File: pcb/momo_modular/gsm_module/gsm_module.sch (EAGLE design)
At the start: 19 parts, among them U1 PIC16LF1823, U2 TI-HIGHSIDE-PFET, U3 SIM900, U4 ESD-SMF05C

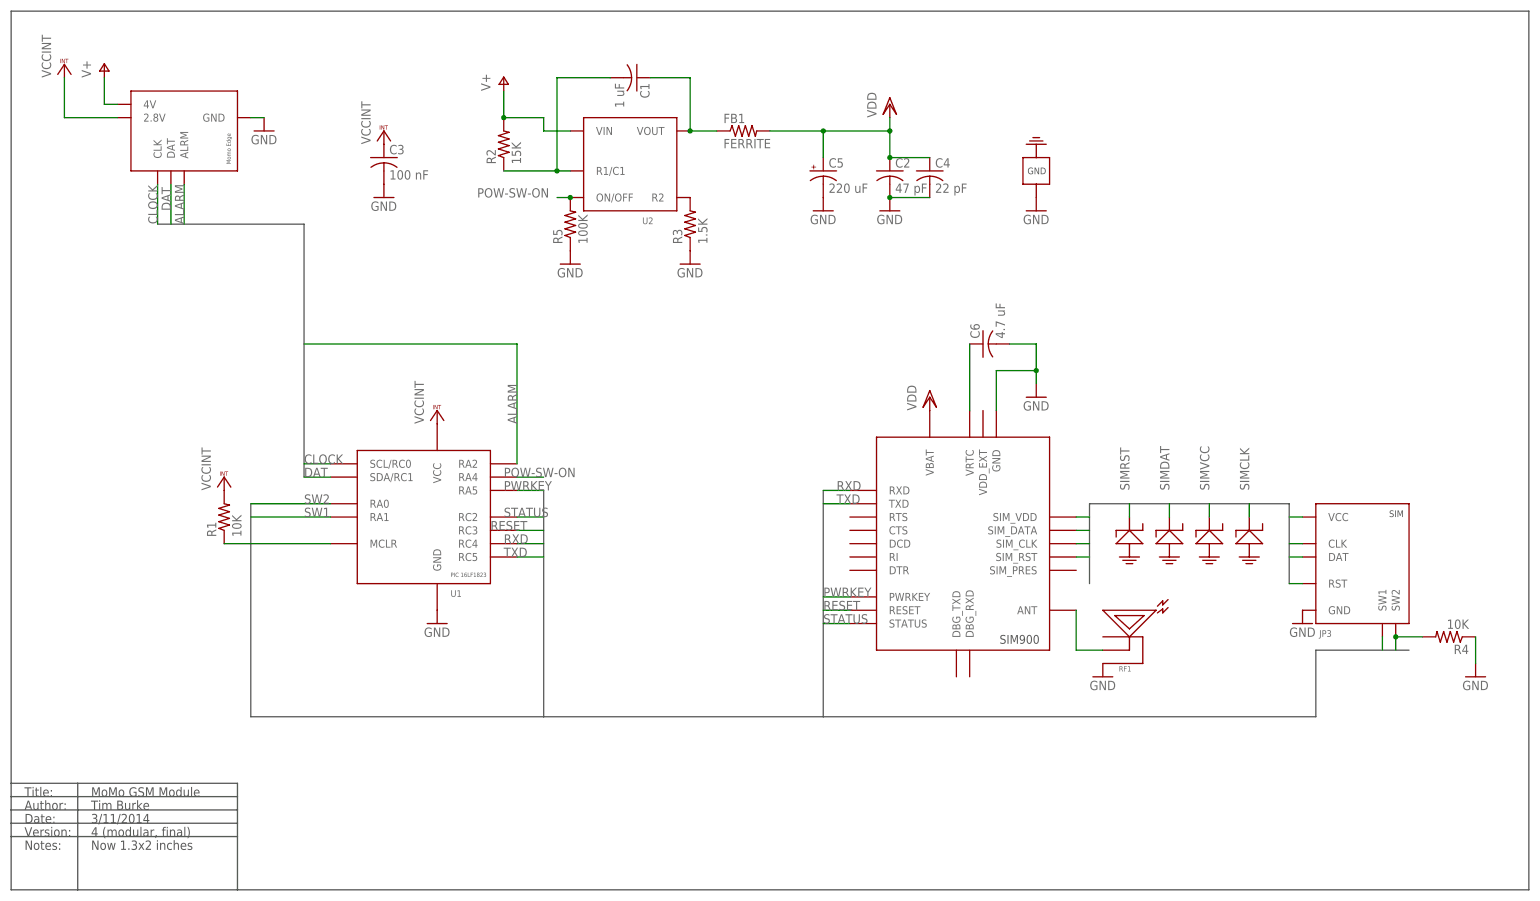
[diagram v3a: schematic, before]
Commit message: Revise GSM module to include pic16lf1847, microsim
Also updated layout for better reflow and moved
traces further from board edges.
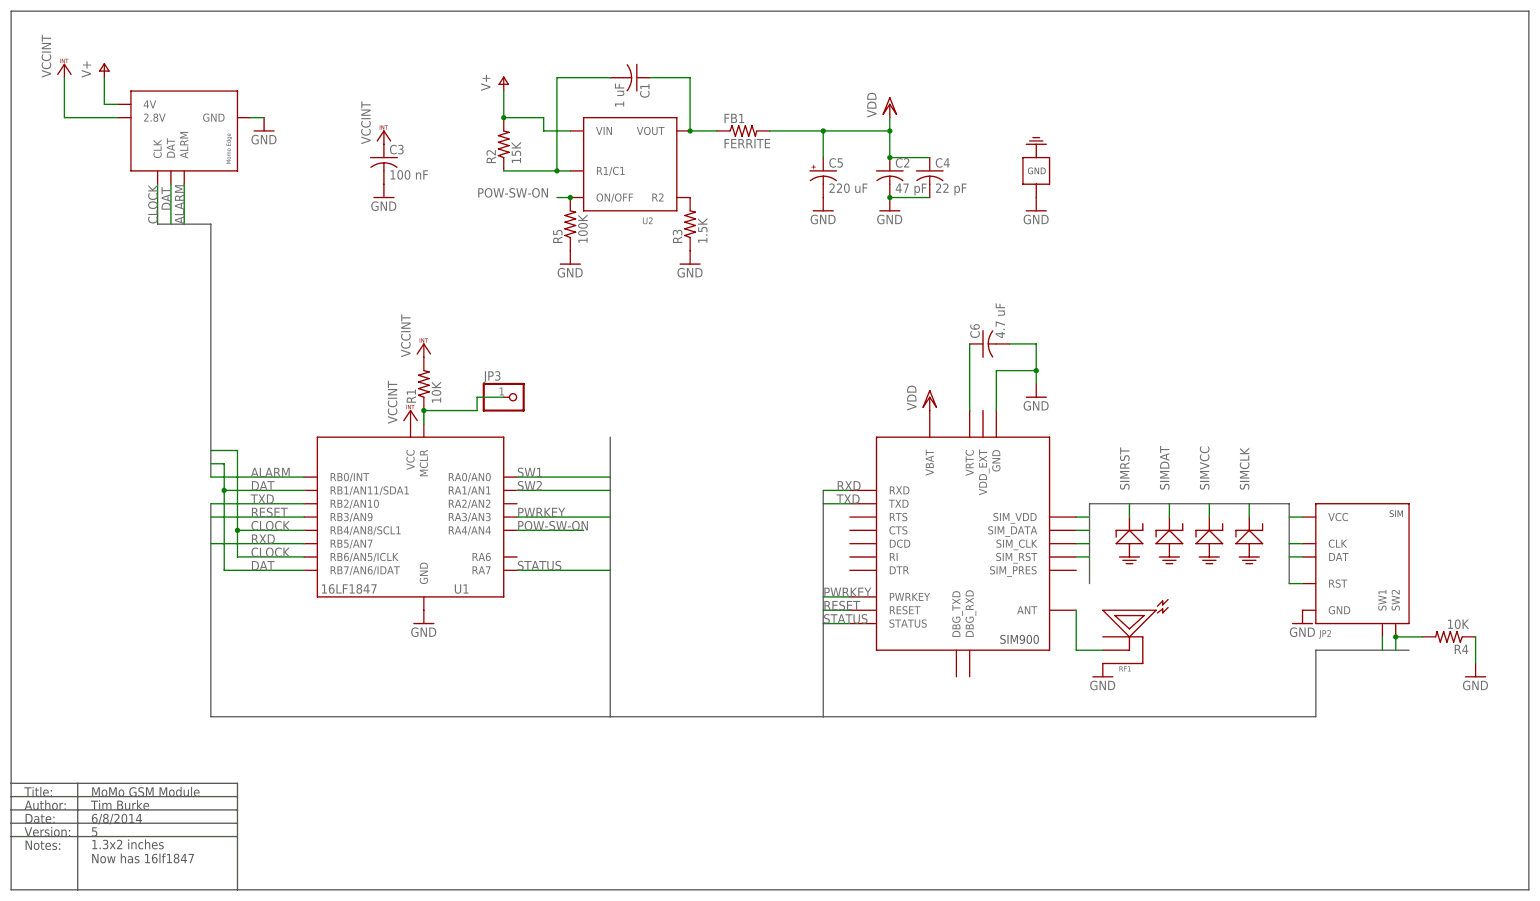
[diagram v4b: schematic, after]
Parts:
- added JP2: SIMHOLDER-8PINMICROSIM, components:SIMHOLDER-8PINMICROSIM
- JP3: value SIMHOLDER-8PINHING -> (none); device components:SIMHOLDER-8PINHING -> pinhead:PINHD-1X1
- U1: value PIC16LF1823 -> PIC16LF1847; device components:PIC16LF1823 -> components:PIC16LF1847; DIGIKEY-PN PIC16LF1823-I/SL-ND -> (none)
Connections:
- removed net N$6: R1.1, U1.MCLR
- new net N$2: JP3.1, R1.1, U1.MCLR
- net ALARM: now also U1.RB0/INT; no longer U1.RA2
- net CLOCK: now also U1.RB4/AN8/SCL1, U1.RB6/AN5/ICLK; no longer U1.SCL/RC0
- net DAT: now also U1.RB1/AN11/SDA1, U1.RB7/AN6/IDAT; no longer U1.SDA/RC1
- net GND: now also JP2.GND; no longer JP3.GND
- net POW-SW-ON: now also U1.RA4/AN4; no longer U1.RA4
- net PWRKEY: now also U1.RA3/AN3; no longer U1.RA5
- net RESET: now also U1.RB3/AN9; no longer U1.RC3
- net RXD: now also U1.RB5/AN7; no longer U1.RC4
- net SIMCLK: now also JP2.CLK; no longer JP3.CLK
- net SIMDAT: now also JP2.DAT; no longer JP3.DAT
- net SIMRST: now also JP2.RST; no longer JP3.RST
- net SIMVCC: now also JP2.VCC; no longer JP3.VCC
- net STATUS: now also U1.RA7; no longer U1.RC2
- net SW1: now also JP2.SW1, U1.RA0/AN0; no longer JP3.SW1, U1.RA1
- net SW2: now also JP2.SW2, U1.RA1/AN1; no longer JP3.SW2, U1.RA0
- net TXD: now also U1.RB2/AN10; no longer U1.RC5
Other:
- note added: "1.3x2 inches Now has 16lf1847"
- note added: "5"
- note added: "6/8/2014"
- note removed: "3/11/2014"
- note removed: "4 (modular, final)"
- note removed: "Now 1.3x2 inches"
- moved on the sheet: R1
